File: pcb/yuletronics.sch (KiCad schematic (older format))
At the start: 35 parts, among them IC1 STM32F042F6P6, IC2 MCP1700, IC3 TLV61225, J1 BATT, J2 MICROUSB, P1 SWD_TC, SW1 BOOTLOAD, SW2 PWR_SWITCH

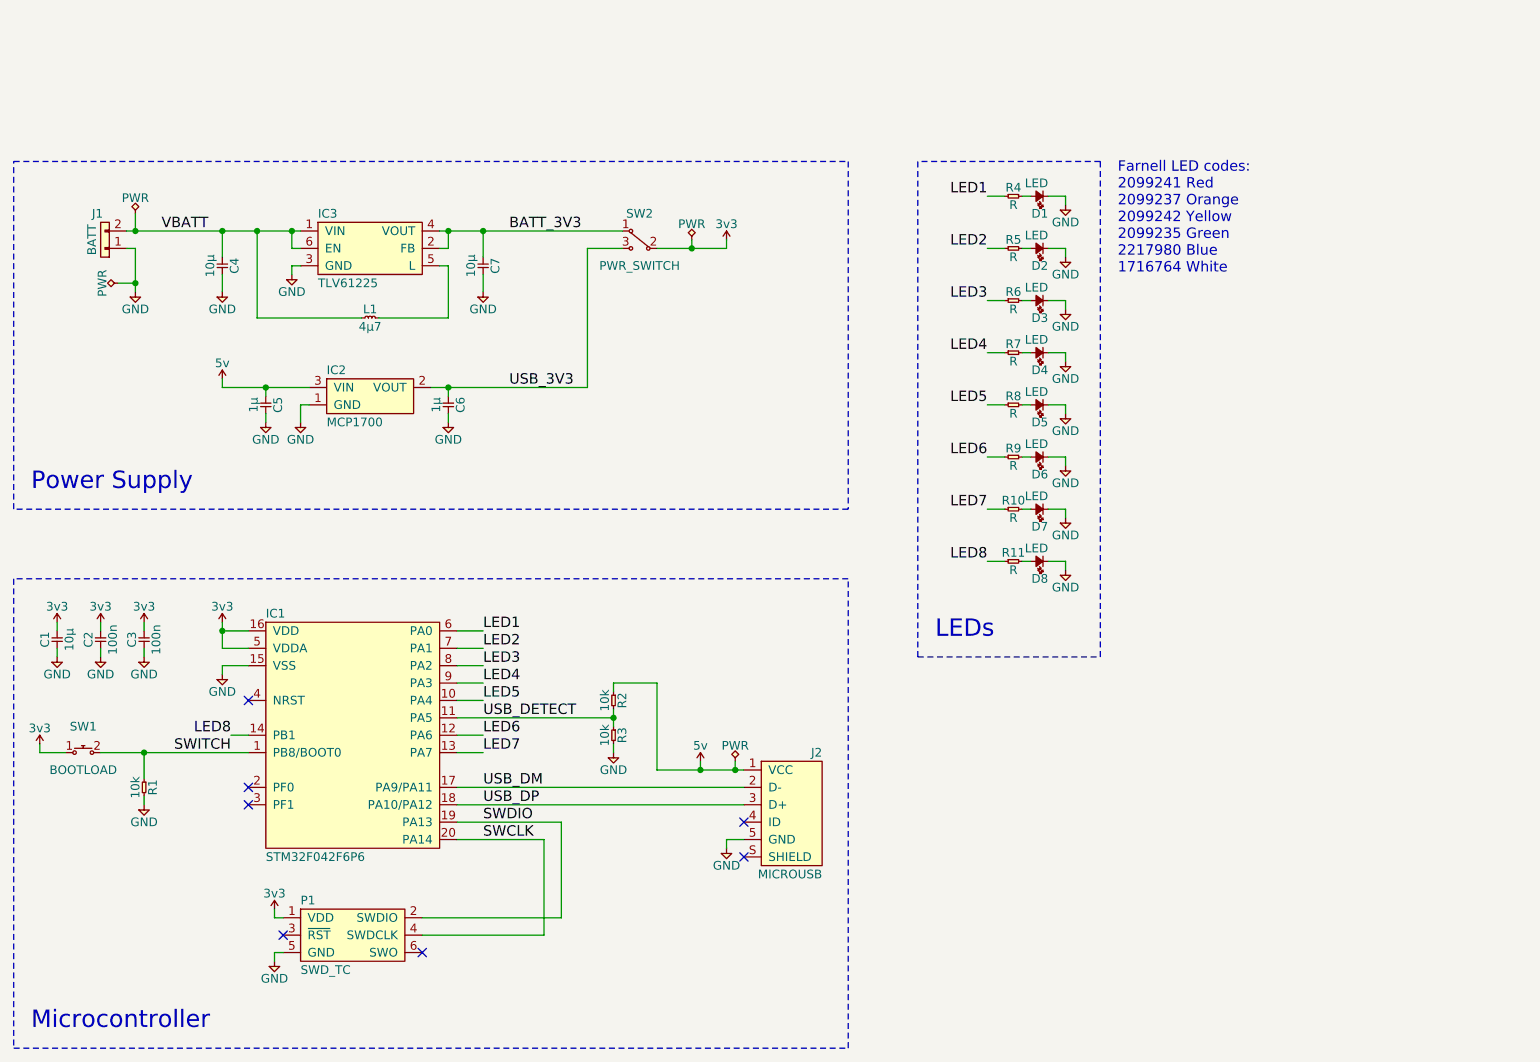
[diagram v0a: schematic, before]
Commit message: Add LED array
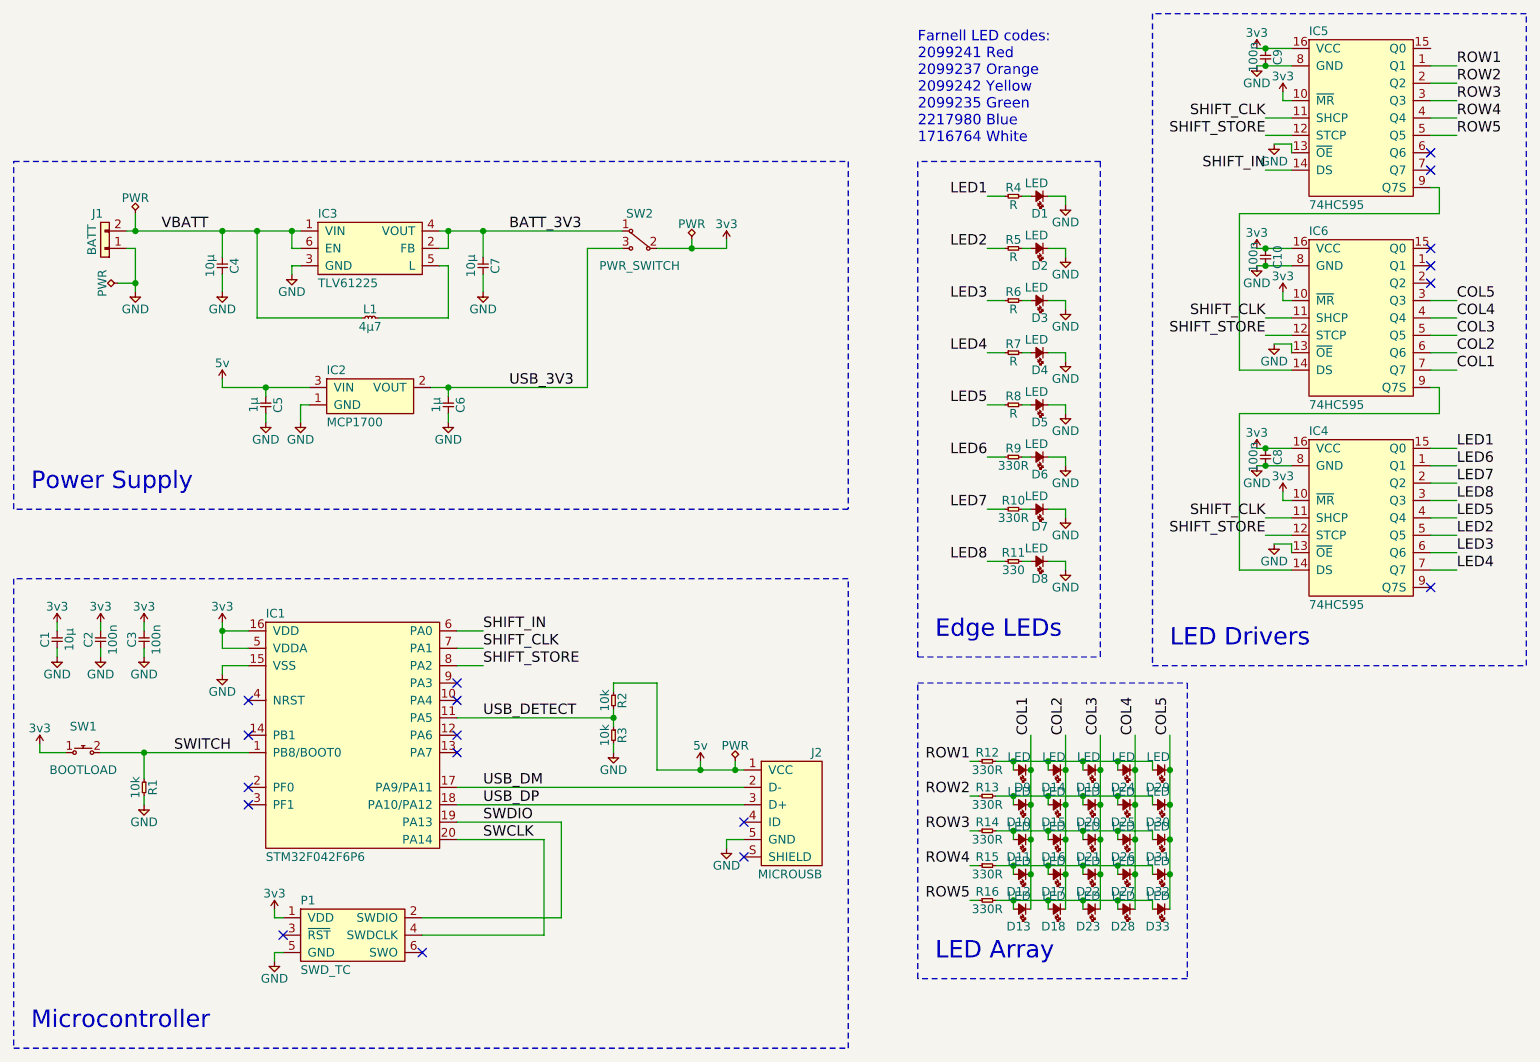
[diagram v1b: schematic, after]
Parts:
- added C10, C8, C9: 100n, agg:0603, symbol C
- added D10, D11, D12, D13, D14, D15, D16, D17, D18, D19, D20, D21, D22, D23, D24, D25, D26, D27, D28, D29, D30, D31, D32, D33, D9: LED, kpt-1608:KPT-1608, symbol LED
- added IC4, IC5, IC6: 74HC595, agg:TSSOP-16, symbol 74HC595
- added R12, R13, R14, R15, R16: 330R, agg:0603, symbol R
- R10, R9: value R -> 330R; footprint agg:0805 -> agg:0603
- R11: value R -> 330; footprint agg:0805 -> agg:0603
- R4, R5, R6, R7, R8: footprint agg:0805 -> agg:0603
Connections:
- net 3v3: now also C10.1, C8.1, C9.1, IC4.10 (~MR), IC4.16 (VCC), IC5.10 (~MR), IC5.16 (VCC), IC6.10 (~MR), IC6.16 (VCC)
- net GND: now also C10.2, C8.2, C9.2, IC4.13 (~OE), IC4.8 (GND), IC5.13 (~OE), IC5.8 (GND), IC6.13 (~OE), IC6.8 (GND)
- net LED1: now also IC4.15 (Q0); no longer IC1.6 (PA0)
- net LED2: now also IC4.5 (Q5); no longer IC1.7 (PA1)
- net LED3: now also IC4.6 (Q6); no longer IC1.8 (PA2)
- net LED4: now also IC4.7 (Q7); no longer IC1.9 (PA3)
- net LED5: now also IC4.4 (Q4); no longer IC1.10 (PA4)
- net LED6: now also IC4.1 (Q1); no longer IC1.12 (PA6)
- net LED7: now also IC4.2 (Q2); no longer IC1.13 (PA7)
- net LED8: now also IC4.3 (Q3); no longer IC1.14 (PB1)
- new net: IC4.14 (DS), IC6.9 (Q7S)
- new net: IC5.9 (Q7S), IC6.14 (DS)
- new net: D14.2, D19.2, D24.2, D29.2, D9.2, R12.2
- new net: D10.2, D15.2, D20.2, D25.2, D30.2, R13.2
- new net: D11.2, D16.2, D21.2, D26.2, D31.2, R14.2
- new net: D12.2, D17.2, D22.2, D27.2, D32.2, R15.2
- new net: D13.2, D18.2, D23.2, D28.2, D33.2, R16.2
- new net COL1: D10.1, D11.1, D12.1, D13.1, D9.1, IC6.7 (Q7)
- new net COL2: D14.1, D15.1, D16.1, D17.1, D18.1, IC6.6 (Q6)
- new net COL3: D19.1, D20.1, D21.1, D22.1, D23.1, IC6.5 (Q5)
- new net COL4: D24.1, D25.1, D26.1, D27.1, D28.1, IC6.4 (Q4)
- new net COL5: D29.1, D30.1, D31.1, D32.1, D33.1, IC6.3 (Q3)
- new net ROW1: IC5.1 (Q1), R12.1
- new net ROW2: IC5.2 (Q2), R13.1
- new net ROW3: IC5.3 (Q3), R14.1
- new net ROW4: IC5.4 (Q4), R15.1
- new net ROW5: IC5.5 (Q5), R16.1
- new net SHIFT_CLK: IC1.7 (PA1), IC4.11 (SHCP), IC5.11 (SHCP), IC6.11 (SHCP)
- new net SHIFT_IN: IC1.6 (PA0), IC5.14 (DS)
- new net SHIFT_STORE: IC1.8 (PA2), IC4.12 (STCP), IC5.12 (STCP), IC6.12 (STCP)
- no-connect marks 7 -> 18
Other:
- note added: "Edge LEDs"
- note added: "LED Array"
- note added: "LED Drivers"
- note removed: "LEDs"

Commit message: Add gerbers, fix DRC
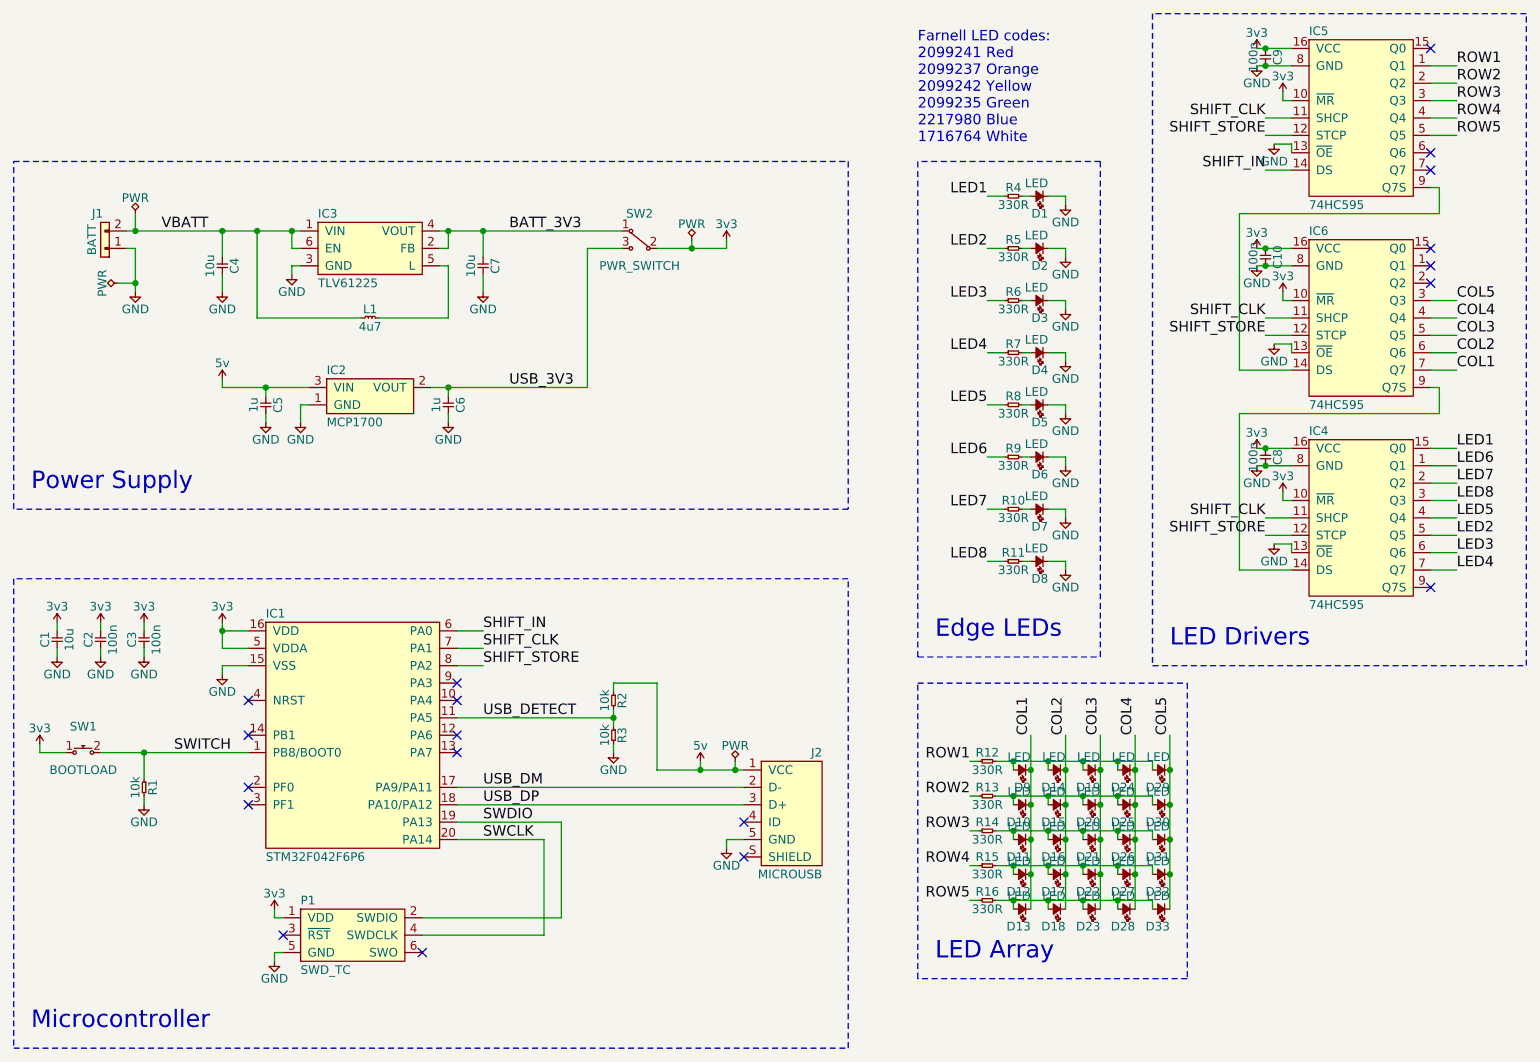
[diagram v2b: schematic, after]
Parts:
- C1, C4, C7: value 10µ -> 10u; footprint agg:0805 -> agg:0603; Farnell 2320851 -> 2494230
- C10, C8, C9: Farnell (none) -> 1759038
- C2, C3: footprint agg:0805 -> agg:0603; Farnell 1759265 -> 1759038
- C5, C6: value 1µ -> 1u; footprint agg:0805 -> agg:0603; Farnell 2320853 -> 1759399
- D1: Farnell 2099241 -> 2099242
- D2: Farnell 2099235 -> 2217980
- D3: Farnell 2099241 -> 2099235
- D4: footprint agg:0805-LED -> kpa-1606:KPA-1606; Farnell 2099235 -> 2290355
- D5: Farnell 2099241 -> 2217980
- D6: footprint agg:0805-LED -> kpa-1606:KPA-1606; Farnell 2099235 -> 2290360
- D8: Farnell 2099235 -> 2099242
- L1: value 4µ7 -> 4u7
- R1, R2, R3: footprint agg:0805 -> agg:0603; Farnell 9332391 -> 9330399
- R10, R12, R13, R14, R15, R16, R9: Farnell (none) -> 9331018
- R11: value 330 -> 330R; Farnell (none) -> 9331018
- R4, R5, R6, R7, R8: value R -> 330R; Farnell (none) -> 9331018
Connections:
- no-connect marks 18 -> 19
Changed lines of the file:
@@
 F 0 "C3" H 2200 4670 50  0000 C CNN
 F 1 "100n" H 2200 4530 50  0000 C CNN
-F 2 "agg:0805" H 2150 4600 50  0001 C CNN
+F 2 "agg:0603" H 2150 4600 50  0001 C CNN
 F 3 "" H 2150 4600 50  0001 C CNN
-F 4 "1759265" H 2150 4600 60  0001 C CNN "Farnell"
+F 4 "1759038" H 2150 4600 60  0001 C CNN "Farnell"
 	1    2150 4600
 	0    -1   -1   0
@@
 F 0 "C2" H 1950 4670 50  0000 C CNN
 F 1 "100n" H 1950 4530 50  0000 C CNN
-F 2 "agg:0805" H 1900 4600 50  0001 C CNN
+F 2 "agg:0603" H 1900 4600 50  0001 C CNN
 F 3 "" H 1900 4600 50  0001 C CNN
-F 4 "1759265" H 1900 4600 60  0001 C CNN "Farnell"
+F 4 "1759038" H 1900 4600 60  0001 C CNN "Farnell"
 	1    1900 4600
 	0    -1   -1   0
@@
 P 1650 4600
 F 0 "C1" H 1700 4670 50  0000 C CNN
-F 1 "10µ" H 1700 4530 50  0000 C CNN
-F 2 "agg:0805" H 1650 4600 50  0001 C CNN
+F 1 "10u" H 1700 4530 50  0000 C CNN
+F 2 "agg:0603" H 1650 4600 50  0001 C CNN
 F 3 "" H 1650 4600 50  0001 C CNN
-F 4 "2320851" H 1650 4600 60  0001 C CNN "Farnell"
+F 4 "2494230" H 1650 4600 60  0001 C CNN "Farnell"
 	1    1650 4600
 	0    -1   -1   0
@@
 F 2 "agg:0805-LED" H 7350 2000 50  0001 C CNN
 F 3 "" H 7350 2000 50  0001 C CNN
-F 4 "2099241" H 7350 2000 60  0001 C CNN "Farnell"
+F 4 "2099242" H 7350 2000 60  0001 C CNN "Farnell"
 	1    7350 2000
 	-1   0    0    1
@@
 P 7100 2000
 F 0 "R4" H 7150 2050 50  0000 C CNN
-F 1 "R" H 7150 1950 50  0000 C CNN
+F 1 "330R" H 7150 1950 50  0000 C CNN
 F 2 "agg:0603" H 7100 2000 50  0001 C CNN
 F 3 "" H 7100 2000 50  0001 C CNN
+F 4 "9331018" H 7100 2000 60  0001 C CNN "Farnell"
 	1    7100 2000
 	1    0    0    -1
@@
 P 2600 2350
 F 0 "C4" H 2650 2420 50  0000 C CNN
-F 1 "10µ" H 2650 2280 50  0000 C CNN
-F 2 "agg:0805" H 2600 2350 50  0001 C CNN
+F 1 "10u" H 2650 2280 50  0000 C CNN
+F 2 "agg:0603" H 2600 2350 50  0001 C CNN
 F 3 "" H 2600 2350 50  0001 C CNN
-F 4 "2320851" H 2600 2350 60  0001 C CNN "Farnell"
+F 4 "2494230" H 2600 2350 60  0001 C CNN "Farnell"
 	1    2600 2350
 	0    1    1    0
@@
 P 4100 2350
 F 0 "C7" H 4150 2420 50  0000 C CNN
-F 1 "10µ" H 4150 2280 50  0000 C CNN
-F 2 "agg:0805" H 4100 2350 50  0001 C CNN
+F 1 "10u" H 4150 2280 50  0000 C CNN
+F 2 "agg:0603" H 4100 2350 50  0001 C CNN
 F 3 "" H 4100 2350 50  0001 C CNN
-F 4 "2320851" H 4100 2350 60  0001 C CNN "Farnell"
+F 4 "2494230" H 4100 2350 60  0001 C CNN "Farnell"
 	1    4100 2350
 	0    1    1    0
@@
 P 3400 2700
 F 0 "L1" H 3450 2750 50  0000 C CNN
-F 1 "4µ7" H 3450 2650 50  0000 C CNN
+F 1 "4u7" H 3450 2650 50  0000 C CNN
 F 2 "agg:2016M" H 3400 2700 50  0001 C CNN
 F 3 "http://www.farnell.com/datasheets/2113219.pdf" H 3400 2700 50  0001 C CNN
@@
 F 0 "R1" H 2200 5400 50  0000 C CNN
 F 1 "10k" H 2200 5300 50  0000 C CNN
-F 2 "agg:0805" H 2150 5350 50  0001 C CNN
+F 2 "agg:0603" H 2150 5350 50  0001 C CNN
 F 3 "" H 2150 5350 50  0001 C CNN
-F 4 "9332391" H 2150 5350 60  0001 C CNN "Farnell"
+F 4 "9330399" H 2150 5350 60  0001 C CNN "Farnell"
 	1    2150 5350
 	0    1    1    0
@@
 F 0 "R2" H 4900 4900 50  0000 C CNN
 F 1 "10k" H 4900 4800 50  0000 C CNN
-F 2 "agg:0805" H 4850 4850 50  0001 C CNN
+F 2 "agg:0603" H 4850 4850 50  0001 C CNN
 F 3 "" H 4850 4850 50  0001 C CNN
-F 4 "9332391" H 4850 4850 60  0001 C CNN "Farnell"
+F 4 "9330399" H 4850 4850 60  0001 C CNN "Farnell"
 	1    4850 4850
 	0    1    1    0
@@
 F 0 "R3" H 4900 5100 50  0000 C CNN
 F 1 "10k" H 4900 5000 50  0000 C CNN
-F 2 "agg:0805" H 4850 5050 50  0001 C CNN
+F 2 "agg:0603" H 4850 5050 50  0001 C CNN
 F 3 "" H 4850 5050 50  0001 C CNN
-F 4 "9332391" H 4850 5050 60  0001 C CNN "Farnell"
+F 4 "9330399" H 4850 5050 60  0001 C CNN "Farnell"
 	1    4850 5050
 	0    1    1    0
@@
 F 2 "agg:0805-LED" H 7350 2300 50  0001 C CNN
 F 3 "" H 7350 2300 50  0001 C CNN
-F 4 "2099235" H 7350 2300 60  0001 C CNN "Farnell"
+F 4 "2217980" H 7350 2300 60  0001 C CNN "Farnell"
 	1    7350 2300
 	-1   0    0    1
@@
 P 7100 2300
 F 0 "R5" H 7150 2350 50  0000 C CNN
-F 1 "R" H 7150 2250 50  0000 C CNN
+F 1 "330R" H 7150 2250 50  0000 C CNN
 F 2 "agg:0603" H 7100 2300 50  0001 C CNN
 F 3 "" H 7100 2300 50  0001 C CNN
+F 4 "9331018" H 7100 2300 60  0001 C CNN "Farnell"
 	1    7100 2300
 	1    0    0    -1
@@
 F 2 "agg:0805-LED" H 7350 2600 50  0001 C CNN
 F 3 "" H 7350 2600 50  0001 C CNN
-F 4 "2099241" H 7350 2600 60  0001 C CNN "Farnell"
+F 4 "2099235" H 7350 2600 60  0001 C CNN "Farnell"
 	1    7350 2600
 	-1   0    0    1
@@
 P 7100 2600
 F 0 "R6" H 7150 2650 50  0000 C CNN
-F 1 "R" H 7150 2550 50  0000 C CNN
+F 1 "330R" H 7150 2550 50  0000 C CNN
 F 2 "agg:0603" H 7100 2600 50  0001 C CNN
 F 3 "" H 7100 2600 50  0001 C CNN
+F 4 "9331018" H 7100 2600 60  0001 C CNN "Farnell"
 	1    7100 2600
 	1    0    0    -1
@@
 F 0 "D4" H 7350 3000 50  0000 L CNN
 F 1 "LED" H 7350 2825 50  0000 L CNN
-F 2 "agg:0805-LED" H 7350 2900 50  0001 C CNN
+F 2 "kpa-1606:KPA-1606" H 7350 2900 50  0001 C CNN
 F 3 "" H 7350 2900 50  0001 C CNN
-F 4 "2099235" H 7350 2900 60  0001 C CNN "Farnell"
+F 4 "2290355" H 7350 2900 60  0001 C CNN "Farnell"
 	1    7350 2900
 	-1   0    0    1
@@
 P 7100 2900
 F 0 "R7" H 7150 2950 50  0000 C CNN
-F 1 "R" H 7150 2850 50  0000 C CNN
+F 1 "330R" H 7150 2850 50  0000 C CNN
 F 2 "agg:0603" H 7100 2900 50  0001 C CNN
 F 3 "" H 7100 2900 50  0001 C CNN
+F 4 "9331018" H 7100 2900 60  0001 C CNN "Farnell"
 	1    7100 2900
 	1    0    0    -1
@@
 F 2 "agg:0805-LED" H 7350 3200 50  0001 C CNN
 F 3 "" H 7350 3200 50  0001 C CNN
-F 4 "2099241" H 7350 3200 60  0001 C CNN "Farnell"
+F 4 "2217980" H 7350 3200 60  0001 C CNN "Farnell"
 	1    7350 3200
 	-1   0    0    1
@@
 P 7100 3200
 F 0 "R8" H 7150 3250 50  0000 C CNN
-F 1 "R" H 7150 3150 50  0000 C CNN
+F 1 "330R" H 7150 3150 50  0000 C CNN
 F 2 "agg:0603" H 7100 3200 50  0001 C CNN
 F 3 "" H 7100 3200 50  0001 C CNN
+F 4 "9331018" H 7100 3200 60  0001 C CNN "Farnell"
 	1    7100 3200
 	1    0    0    -1
@@
 F 0 "D6" H 7350 3600 50  0000 L CNN
 F 1 "LED" H 7350 3425 50  0000 L CNN
-F 2 "agg:0805-LED" H 7350 3500 50  0001 C CNN
+F 2 "kpa-1606:KPA-1606" H 7350 3500 50  0001 C CNN
 F 3 "" H 7350 3500 50  0001 C CNN
-F 4 "2099235" H 7350 3500 60  0001 C CNN "Farnell"
+F 4 "2290360" H 7350 3500 60  0001 C CNN "Farnell"
 	1    7350 3500
 	-1   0    0    1
@@
 F 2 "agg:0603" H 7100 3500 50  0001 C CNN
 F 3 "" H 7100 3500 50  0001 C CNN
+F 4 "9331018" H 7100 3500 60  0001 C CNN "Farnell"
 	1    7100 3500
 	1    0    0    -1
@@
 F 2 "agg:0603" H 7100 3800 50  0001 C CNN
 F 3 "" H 7100 3800 50  0001 C CNN
+F 4 "9331018" H 7100 3800 60  0001 C CNN "Farnell"
 	1    7100 3800
 	1    0    0    -1
@@
 F 2 "agg:0805-LED" H 7350 4100 50  0001 C CNN
 F 3 "" H 7350 4100 50  0001 C CNN
-F 4 "2099235" H 7350 4100 60  0001 C CNN "Farnell"
+F 4 "2099242" H 7350 4100 60  0001 C CNN "Farnell"
 	1    7350 4100
 	-1   0    0    1
@@
 P 7100 4100
 F 0 "R11" H 7150 4150 50  0000 C CNN
-F 1 "330" H 7150 4050 50  0000 C CNN
+F 1 "330R" H 7150 4050 50  0000 C CNN
 F 2 "agg:0603" H 7100 4100 50  0001 C CNN
 F 3 "" H 7100 4100 50  0001 C CNN
+F 4 "9331018" H 7100 4100 60  0001 C CNN "Farnell"
 	1    7100 4100
 	1    0    0    -1
@@
 P 2850 3150
 F 0 "C5" H 2900 3220 50  0000 C CNN
-F 1 "1µ" H 2900 3080 50  0000 C CNN
-F 2 "agg:0805" H 2850 3150 50  0001 C CNN
+F 1 "1u" H 2900 3080 50  0000 C CNN
+F 2 "agg:0603" H 2850 3150 50  0001 C CNN
 F 3 "" H 2850 3150 50  0001 C CNN
-F 4 "2320853" H 2850 3150 60  0001 C CNN "Farnell"
+F 4 "1759399" H 2850 3150 60  0001 C CNN "Farnell"
 	1    2850 3150
 	0    1    1    0
@@
 P 3900 3150
 F 0 "C6" H 3950 3220 50  0000 C CNN
-F 1 "1µ" H 3950 3080 50  0000 C CNN
-F 2 "agg:0805" H 3900 3150 50  0001 C CNN
+F 1 "1u" H 3950 3080 50  0000 C CNN
+F 2 "agg:0603" H 3900 3150 50  0001 C CNN
 F 3 "" H 3900 3150 50  0001 C CNN
-F 4 "2320853" H 3900 3150 60  0001 C CNN "Farnell"
+F 4 "1759399" H 3900 3150 60  0001 C CNN "Farnell"
 	1    3900 3150
 	0    1    1    0
@@
 F 2 "agg:0603" H 8600 3450 50  0001 C CNN
 F 3 "" H 8600 3450 50  0001 C CNN
+F 4 "1759038" H 8600 3450 60  0001 C CNN "Farnell"
 	1    8600 3450
 	0    1    1    0
@@
 F 2 "agg:0603" H 8600 1150 50  0001 C CNN
 F 3 "" H 8600 1150 50  0001 C CNN
+F 4 "1759038" H 8600 1150 60  0001 C CNN "Farnell"
 	1    8600 1150
 	0    1    1    0
@@
 F 2 "agg:0603" H 8600 2300 50  0001 C CNN
 F 3 "" H 8600 2300 50  0001 C CNN
+F 4 "1759038" H 8600 2300 60  0001 C CNN "Farnell"
 	1    8600 2300
 	0    1    1    0
@@
 F 2 "agg:0603" H 6950 5250 50  0001 C CNN
 F 3 "" H 6950 5250 50  0001 C CNN
+F 4 "9331018" H 6950 5250 60  0001 C CNN "Farnell"
 	1    6950 5250
 	1    0    0    -1
@@
 F 2 "agg:0603" H 6950 5450 50  0001 C CNN
 F 3 "" H 6950 5450 50  0001 C CNN
+F 4 "9331018" H 6950 5450 60  0001 C CNN "Farnell"
 	1    6950 5450
 	1    0    0    -1
@@
 F 2 "agg:0603" H 6950 5650 50  0001 C CNN
 F 3 "" H 6950 5650 50  0001 C CNN
+F 4 "9331018" H 6950 5650 60  0001 C CNN "Farnell"
 	1    6950 5650
 	1    0    0    -1
@@
 F 2 "agg:0603" H 6950 5850 50  0001 C CNN
 F 3 "" H 6950 5850 50  0001 C CNN
+F 4 "9331018" H 6950 5850 60  0001 C CNN "Farnell"
 	1    6950 5850
 	1    0    0    -1
@@
 F 2 "agg:0603" H 6950 6050 50  0001 C CNN
 F 3 "" H 6950 6050 50  0001 C CNN
+F 4 "9331018" H 6950 6050 60  0001 C CNN "Farnell"
 	1    6950 6050
 	1    0    0    -1
@@
 Wire Wire Line
 	9600 3100 9550 3100
+NoConn ~ 9550 1150
 $EndSCHEMATC
